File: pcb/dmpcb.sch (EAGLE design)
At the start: 10 parts, among them IC1 7805DT, Q2 IRF530

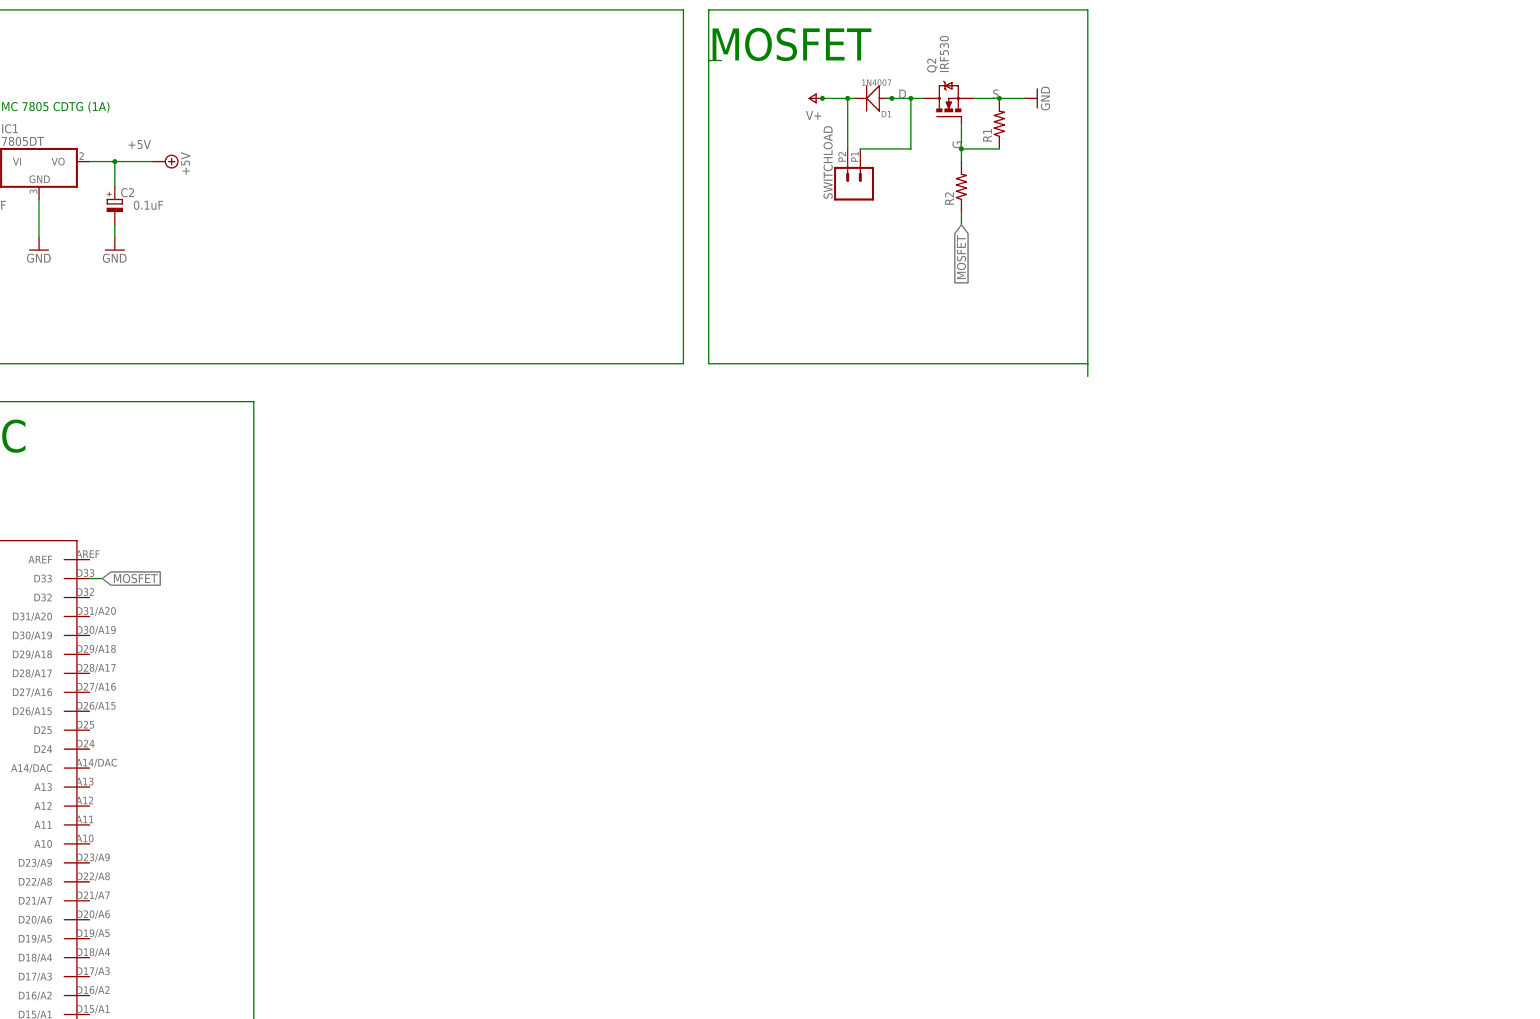
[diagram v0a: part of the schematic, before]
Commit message: added lm293 to schematic
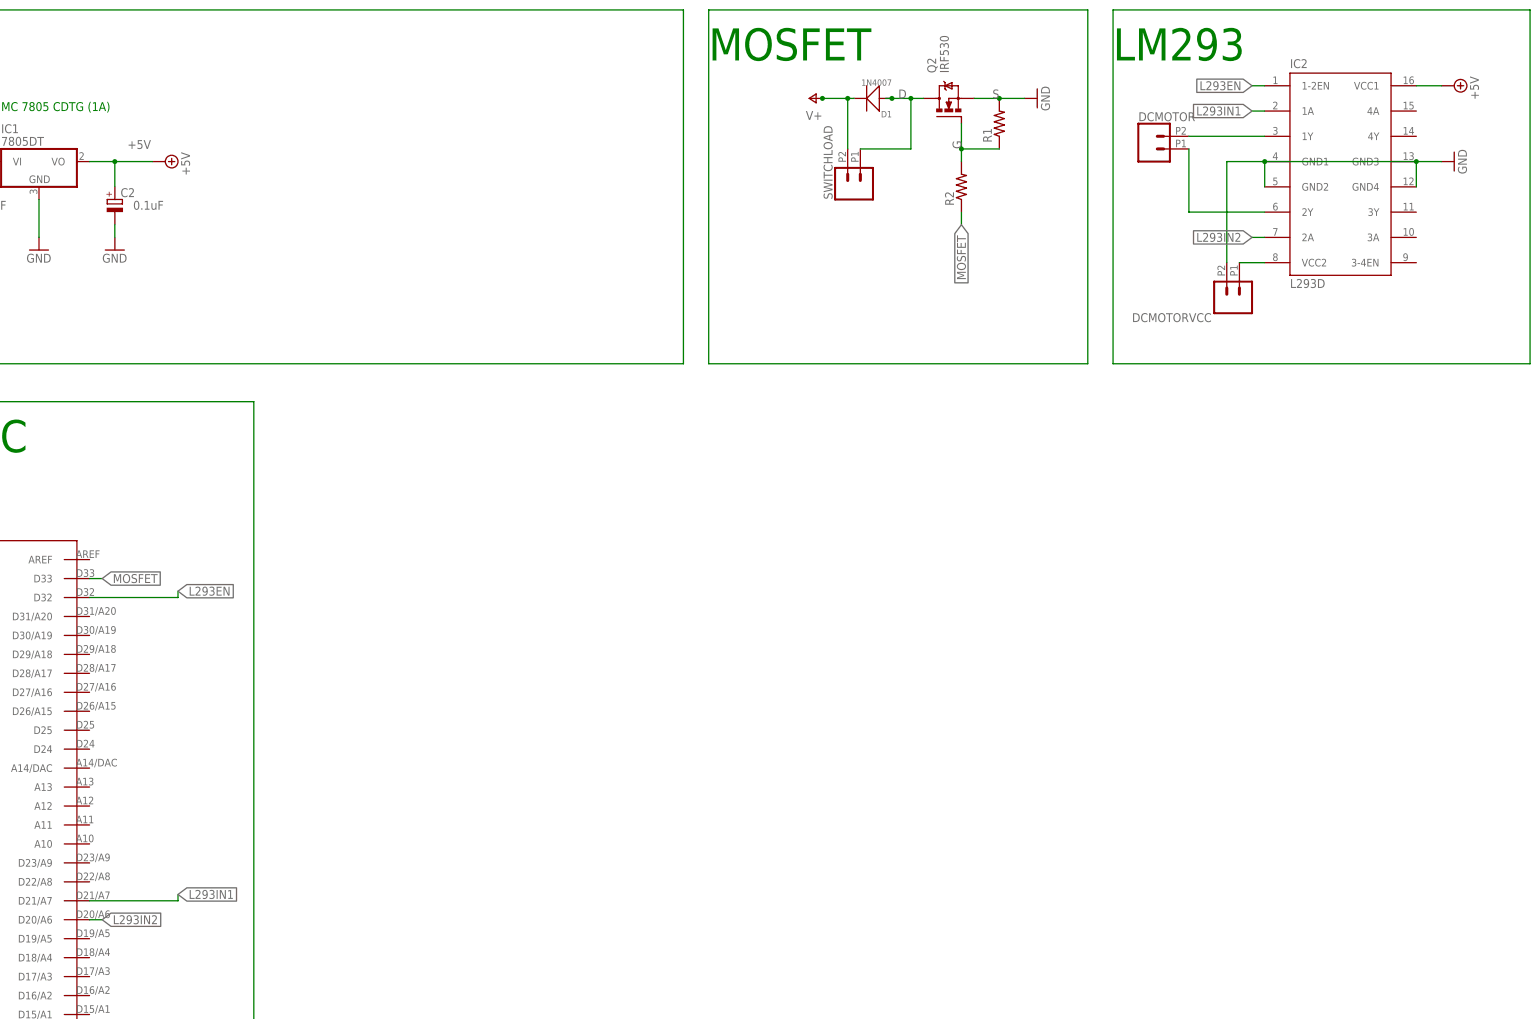
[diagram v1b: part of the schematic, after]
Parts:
- added DCMOTOR, DCMOTORVCC: (no value), SparkFun-Connectors:CONN_022.54MM_SCREWTERM
- added IC2: L293D, st-microelectronics:L293D
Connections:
- new net L293EN: IC2.1-2EN, U$1.D32
- new net L293IN1: IC2.1A, U$1.D21/A7
- new net L293IN2: IC2.2A, U$1.D20/A6
- new net N$4: DCMOTORVCC.1, IC2.VCC2
- new net N$5: DCMOTOR.2, IC2.1Y
- new net N$6: DCMOTOR.1, IC2.2Y
- net +5V: now also IC2.VCC1
- net GND: now also DCMOTORVCC.2, IC2.GND1, IC2.GND2, IC2.GND3, IC2.GND4
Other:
- note added: "LM293"

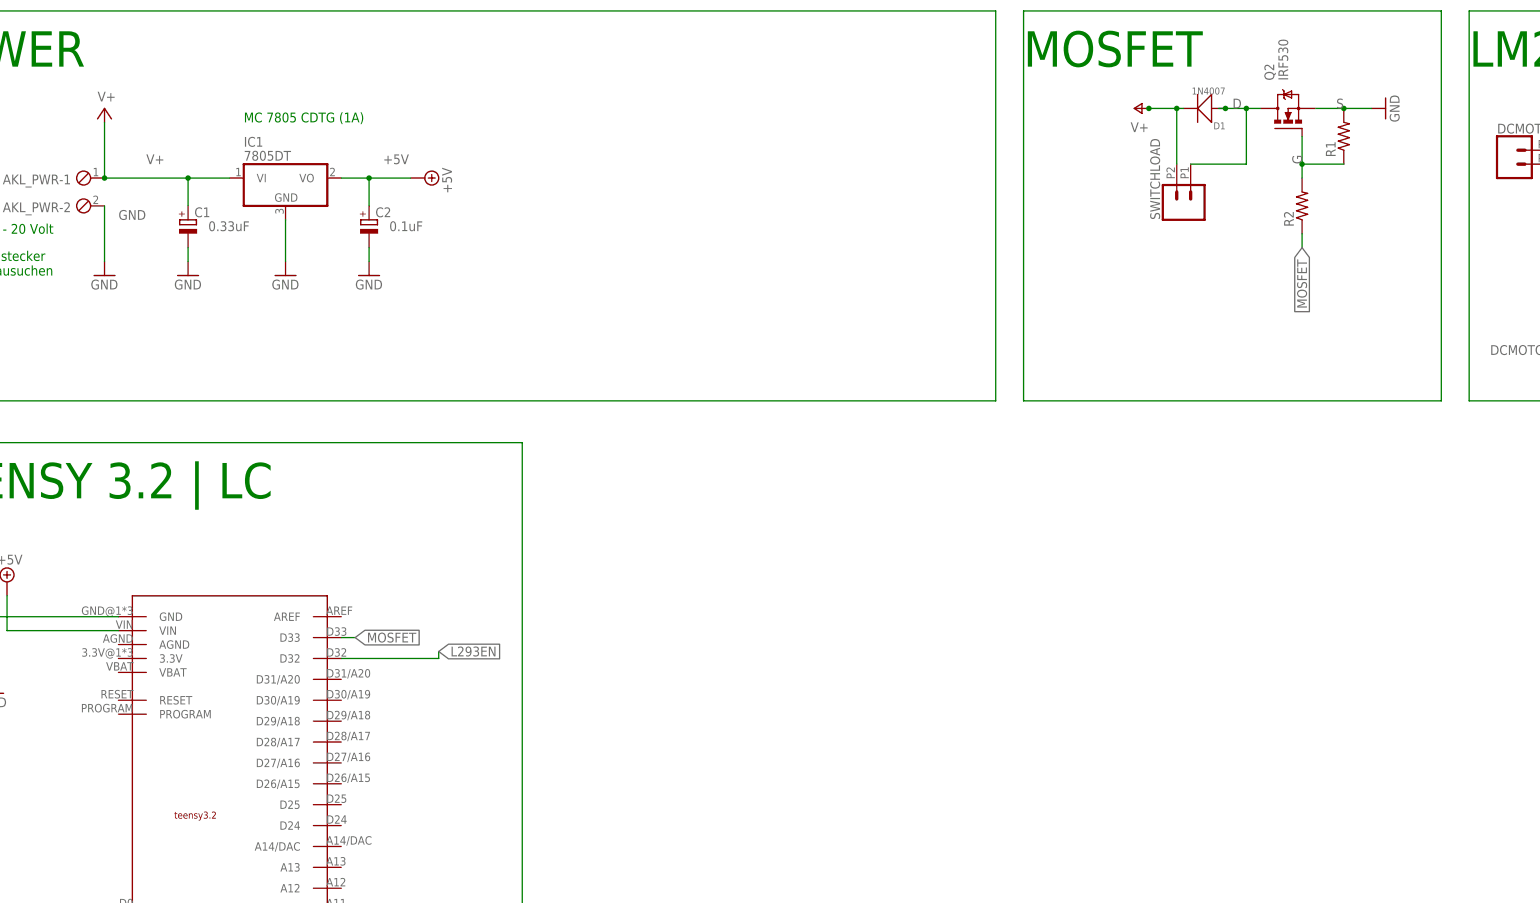
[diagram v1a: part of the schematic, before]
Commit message: added Filtercap, powerled, doubled up the mosfet, also added possiblitiy to jump protectiondiode for mosfets
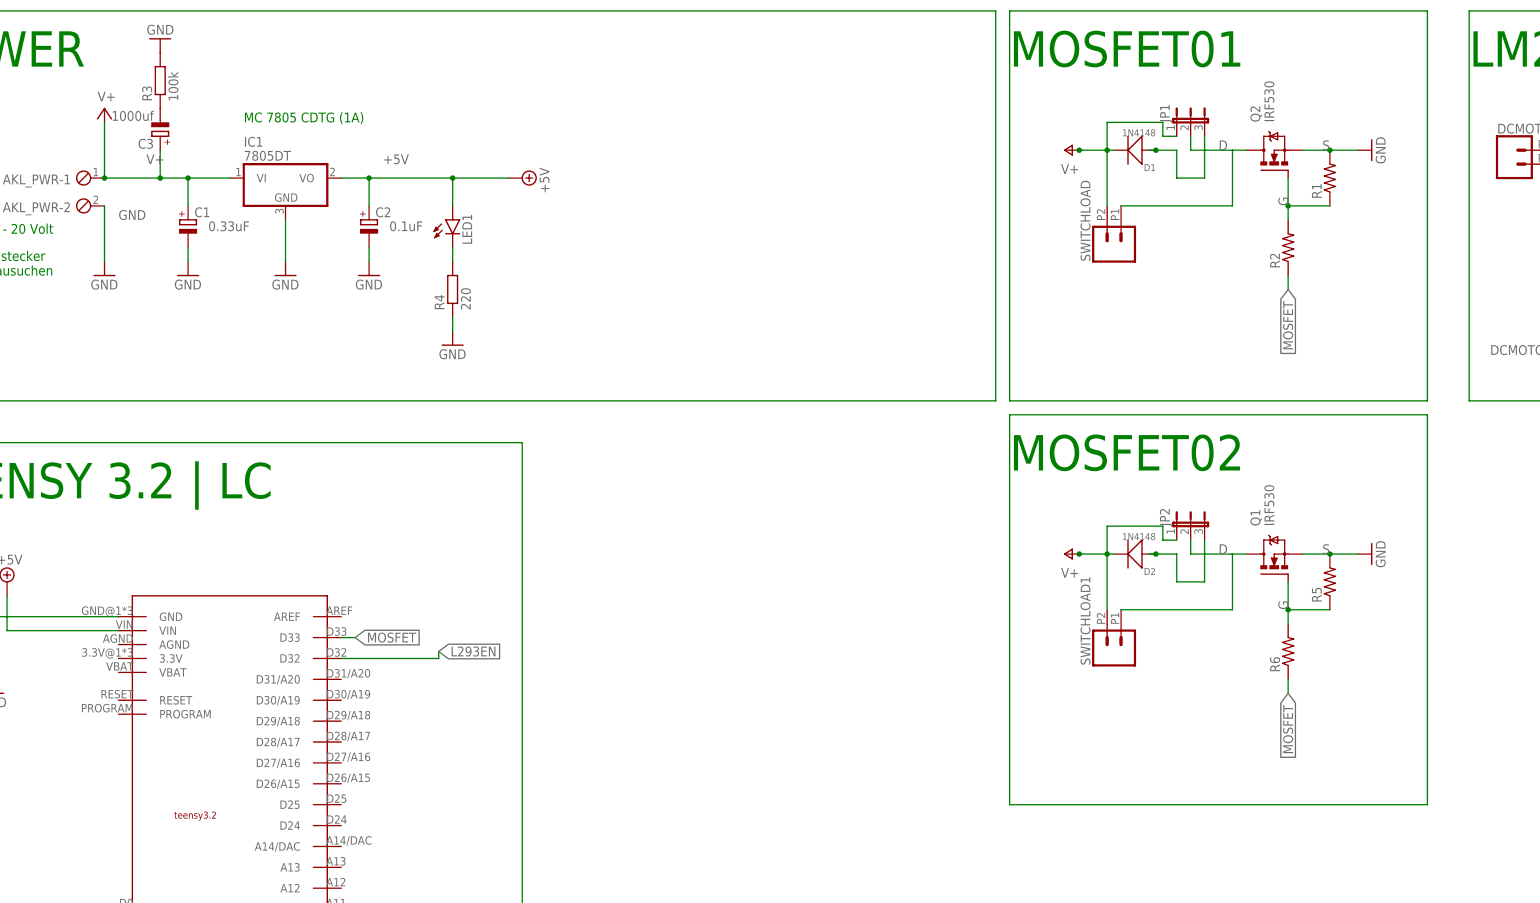
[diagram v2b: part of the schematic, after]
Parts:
- added C3: 1000uf, rcl:CPOL-EUE3.5-8
- added D2: 1N4148, Seeed-Diode:SMD-DIODE-SWITCH-1N4148(LL-34)
- added JP1, JP2: (no value), jumper:JP2E
- added LED1: (no value), led:LEDSML0805
- added Q1: IRF530, transistor-power:IRF530
- added R3: 100k, rcl:R-EU_R0805
- added R4: 220, rcl:R-EU_R0805
- added R5, R6: (no value), resistor:R-US_R0805
- added SWITCHLOAD1: (no value), SparkFun-Connectors:CONN_022.54MM_SCREWTERM
- D1: value 1N4007 -> 1N4148; device Seeed-Diode:DIODE-GEN-PURPOSE-1KV-1A(DO-214AC) -> Seeed-Diode:SMD-DIODE-SWITCH-1N4148(LL-34)
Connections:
- new net N$11: D2.+, JP2.3
- new net N$12: D1.+, JP1.3
- new net N$8: C3.-, R3.1
- new net N$9: LED1.C, R4.2
- net +5V: now also LED1.A
- net D: now also JP1.2, JP2.2, Q1.D, SWITCHLOAD1.1; no longer D1.+
- net G: now also Q1.G, R5.1, R6.2
- net GND: now also R3.2, R4.1
- net MOSFET: now also R6.1
- net S: now also Q1.S, R5.2
- net V+: now also C3.+, D2.-, JP1.1, JP2.1, SWITCHLOAD1.2
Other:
- note added: "MOSFET01"
- note added: "MOSFET02"
- note removed: "MOSFET"
- moved on the sheet: D1, Q2, R1, R2, SWITCHLOAD

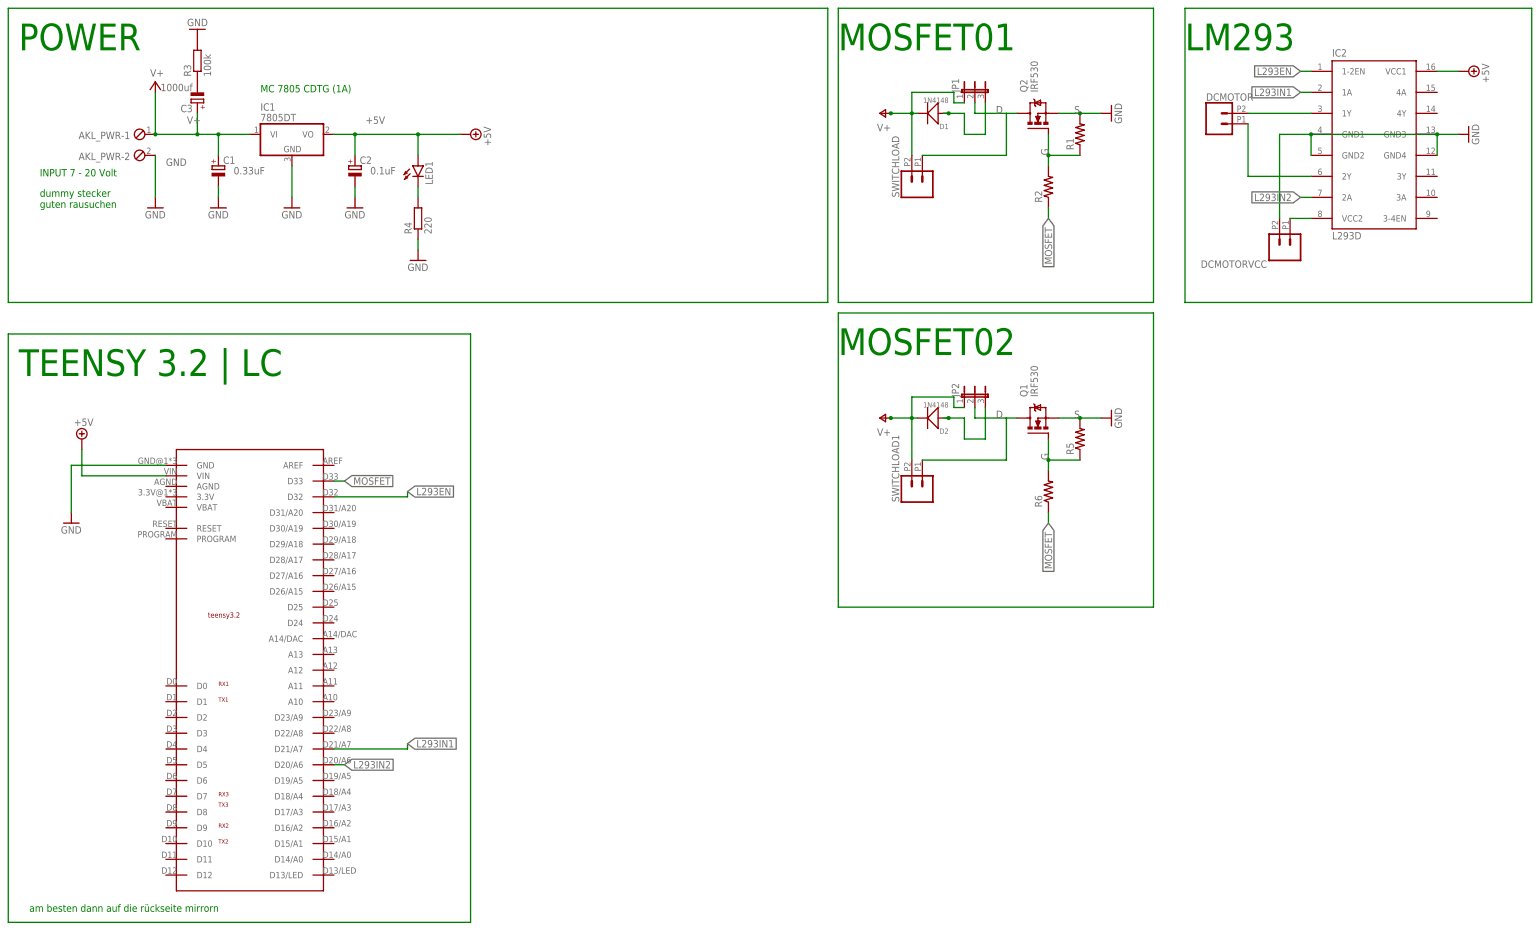
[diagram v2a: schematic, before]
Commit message: added stepperdriver and pots, lm293 still needs some corrections
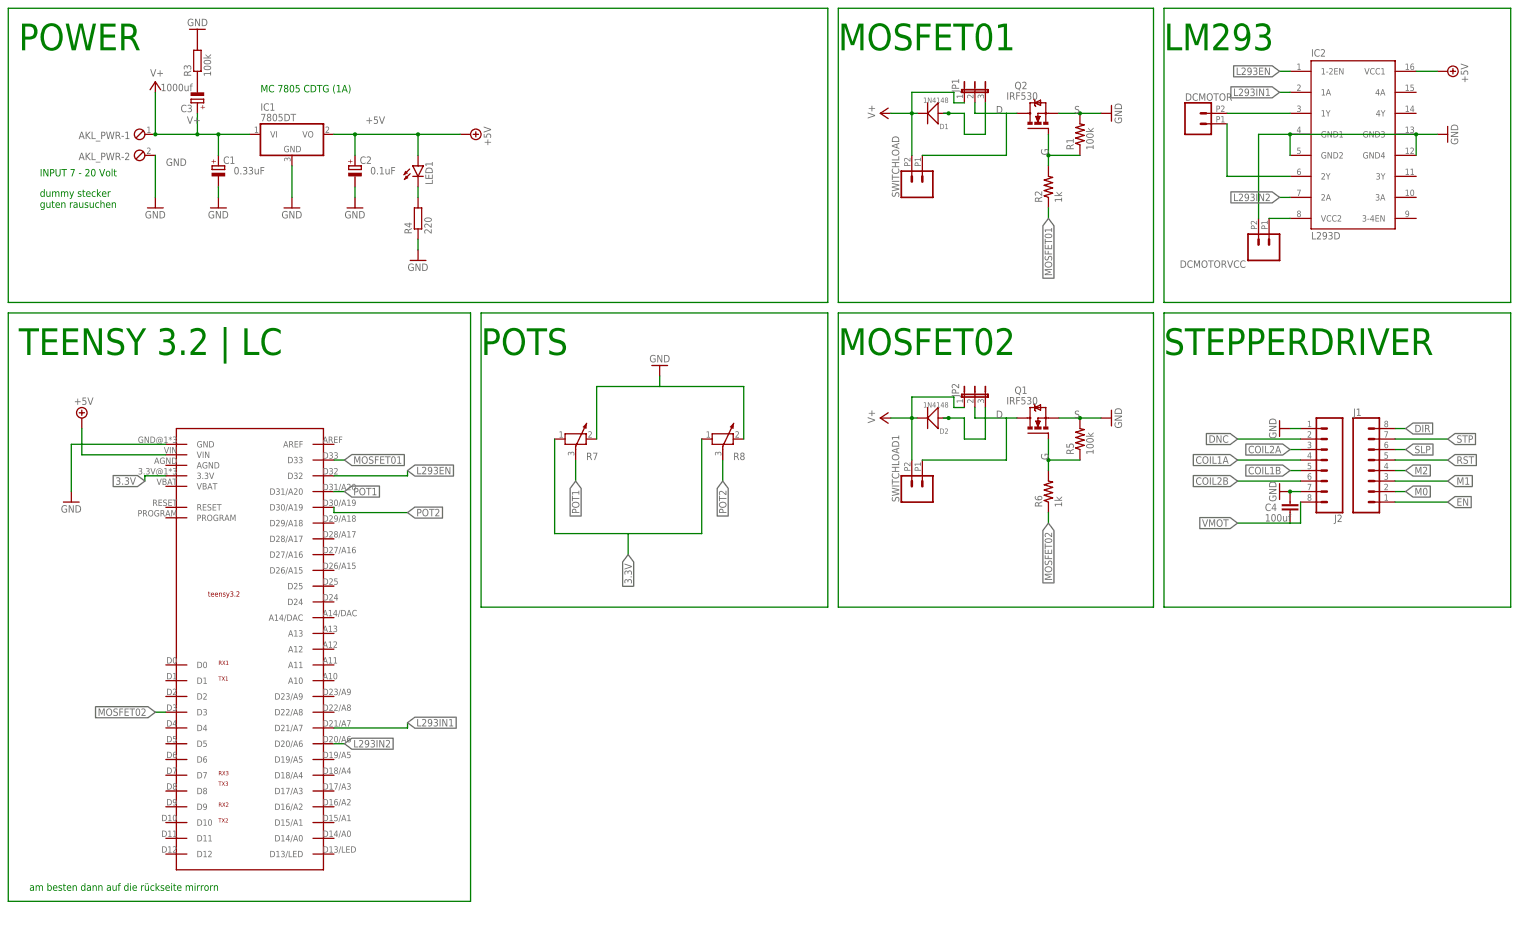
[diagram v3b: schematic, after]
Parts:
- added C4: 100uf, rcl:C-EUC0805
- added J1, J2: (no value), SparkFun-Connectors:CONN_08"
- added R7, R8: (no value), rcl:POTENTIOMETER_PT-10
- R1, R5: value (none) -> 100k
- R2, R6: value (none) -> 1k
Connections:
- removed net MOSFET: R2.1, R6.1, U$1.D33
- new net 3.3V: R7.1, R8.1, U$1.3.3V
- new net COIL1A: J2.4
- new net COIL1B: J2.5
- new net COIL2A: J2.3
- new net COIL2B: J2.6
- new net DIR: J1.8
- new net DNC: J2.2
- new net EN: J1.1
- new net M0: J1.2
- new net M1: J1.3
- new net M2: J1.4
- new net MOSFET01: R2.1, U$1.D33
- new net MOSFET02: R6.1, U$1.D3
- new net POT1: R7.3, U$1.D31/A20
- new net POT2: R8.3, U$1.D30/A19
- new net RST: J1.5
- new net SLP: J1.6
- new net STP: J1.7
- new net VMOT: C4.2, J2.8
- net GND: now also C4.1, J2.1, J2.7, R7.2, R8.2
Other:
- note added: "POTS"
- note added: "STEPPERDRIVER"
- moved on the sheet: DCMOTOR, DCMOTORVCC, IC2
